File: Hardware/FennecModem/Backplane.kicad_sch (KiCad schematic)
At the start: 4 parts, among them U101 NCP1117-12_SOT223

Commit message: Bump backplane
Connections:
- new net SPI_CLK: U302.12 (SPI_CLK)
- new net SPI_SDA1: U302.14 (SPI_SDA1/SPI_SDI)
- new net SPI_SDA2: U302.16 (SPI_SDA2)
- new net SPI_SDA3: U302.18 (SPI_SDA3)
- new net SPI_SDA4: U302.20 (SPI_SDA4)
- no-connect marks 0 -> 7
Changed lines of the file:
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@@
   (junction (at 159.385 88.265) (diameter 0) (color 0 0 0 0)
   )
-  (junction (at 97.155 120.65) (diameter 0) (color 0 0 0 0)
+  (junction (at 97.155 134.62) (diameter 0) (color 0 0 0 0)
   )
   (junction (at 172.72 98.425) (diameter 0) (color 0 0 0 0)
   )
-  (wire (pts (xy 97.155 118.745) (xy 97.155 120.65))
+  (no_connect (at 112.395 122.555))
+  (no_connect (at 112.395 90.805))
+  (no_connect (at 81.915 95.885))
+  (no_connect (at 112.395 93.345))
+  (no_connect (at 81.915 93.345))
+  (no_connect (at 112.395 95.885))
+  (no_connect (at 81.915 90.805))
+  (wire (pts (xy 97.155 132.715) (xy 97.155 134.62))
     (stroke (width 0) (type default))
   )
@@
     (stroke (width 0) (type default))
   )
-  (wire (pts (xy 112.395 93.345) (xy 114.935 93.345))
-    (stroke (width 0) (type default))
-  )
   (wire (pts (xy 159.385 88.265) (xy 159.385 90.805))
     (stroke (width 0) (type default))
   )
-  (wire (pts (xy 99.695 120.65) (xy 99.695 118.745))
+  (wire (pts (xy 112.395 114.935) (xy 114.935 114.935))
+    (stroke (width 0) (type default))
+  )
+  (wire (pts (xy 99.695 134.62) (xy 99.695 132.715))
     (stroke (width 0) (type default))
   )
@@
     (stroke (width 0) (type default))
   )
-  (wire (pts (xy 97.155 120.65) (xy 94.615 120.65))
+  (wire (pts (xy 97.155 134.62) (xy 94.615 134.62))
     (stroke (width 0) (type default))
   )
@@
     (stroke (width 0) (type default))
   )
+  (wire (pts (xy 112.395 102.235) (xy 114.935 102.235))
+    (stroke (width 0) (type default))
+  )
+  (wire (pts (xy 112.395 120.015) (xy 114.935 120.015))
+    (stroke (width 0) (type default))
+  )
   (wire (pts (xy 97.155 76.835) (xy 97.155 80.645))
     (stroke (width 0) (type default))
@@
     (stroke (width 0) (type default))
   )
+  (wire (pts (xy 112.395 104.775) (xy 114.935 104.775))
+    (stroke (width 0) (type default))
+  )
   (wire (pts (xy 140.335 88.265) (xy 159.385 88.265))
     (stroke (width 0) (type default))
   )
-  (wire (pts (xy 112.395 95.885) (xy 114.935 95.885))
-    (stroke (width 0) (type default))
-  )
-  (wire (pts (xy 97.155 120.65) (xy 99.695 120.65))
-    (stroke (width 0) (type default))
-  )
-  (wire (pts (xy 97.155 121.285) (xy 97.155 120.65))
+  (wire (pts (xy 112.395 117.475) (xy 114.935 117.475))
+    (stroke (width 0) (type default))
+  )
+  (wire (pts (xy 112.395 112.395) (xy 114.935 112.395))
+    (stroke (width 0) (type default))
+  )
+  (wire (pts (xy 97.155 134.62) (xy 99.695 134.62))
+    (stroke (width 0) (type default))
+  )
+  (wire (pts (xy 97.155 135.255) (xy 97.155 134.62))
     (stroke (width 0) (type default))
   )
@@
     (stroke (width 0) (type default))
   )
+  (wire (pts (xy 112.395 109.855) (xy 114.935 109.855))
+    (stroke (width 0) (type default))
+  )
   (wire (pts (xy 172.72 98.425) (xy 184.785 98.425))
     (stroke (width 0) (type default))
   )
-  (wire (pts (xy 94.615 118.745) (xy 94.615 120.65))
+  (wire (pts (xy 94.615 132.715) (xy 94.615 134.62))
     (stroke (width 0) (type default))
   )
@@
     (effects (font (size 1.27 1.27)) (justify right bottom))
   )
-  (hierarchical_label "I2C_SCL" (shape input) (at 114.935 93.345 0) (fields_autoplaced)
-    (effects (font (size 1.27 1.27)) (justify left))
-  )
-  (hierarchical_label "I2C_SDA" (shape bidirectional) (at 114.935 95.885 0) (fields_autoplaced)
+  (hierarchical_label "SPI_SDA3" (shape bidirectional) (at 114.935 117.475 0) (fields_autoplaced)
+    (effects (font (size 1.27 1.27)) (justify left))
+  )
+  (hierarchical_label "SPI_SDA2" (shape bidirectional) (at 114.935 114.935 0) (fields_autoplaced)
+    (effects (font (size 1.27 1.27)) (justify left))
+  )
+  (hierarchical_label "SPI_SDA1" (shape bidirectional) (at 114.935 112.395 0) (fields_autoplaced)
+    (effects (font (size 1.27 1.27)) (justify left))
+  )
+  (hierarchical_label "SPI_SDA4" (shape bidirectional) (at 114.935 120.015 0) (fields_autoplaced)
+    (effects (font (size 1.27 1.27)) (justify left))
+  )
+  (hierarchical_label "I2C_SDA" (shape bidirectional) (at 114.935 104.775 0) (fields_autoplaced)
+    (effects (font (size 1.27 1.27)) (justify left))
+  )
+  (hierarchical_label "SPI_CLK" (shape input) (at 114.935 109.855 0) (fields_autoplaced)
+    (effects (font (size 1.27 1.27)) (justify left))
+  )
+  (hierarchical_label "I2C_SCL" (shape input) (at 114.935 102.235 0) (fields_autoplaced)
     (effects (font (size 1.27 1.27)) (justify left))
   )
@@
     )
   )
-  (symbol (lib_id "power:GND") (at 97.155 121.285 0) (unit 1)
+  (symbol (lib_id "power:GND") (at 97.155 135.255 0) (unit 1)
     (in_bom yes) (on_board yes) (dnp no)
-    (property "Reference" "#PWR0116" (at 97.155 127.635 0)
-      (effects (font (size 1.27 1.27)) hide)
-    )
-    (property "Value" "GND" (at 97.155 125.095 0)
+    (property "Reference" "#PWR0116" (at 97.155 141.605 0)
+      (effects (font (size 1.27 1.27)) hide)
+    )
+    (property "Value" "GND" (at 97.155 139.065 0)
       (effects (font (size 1.27 1.27)))
     )
-    (property "Footprint" "" (at 97.155 121.285 0)
-      (effects (font (size 1.27 1.27)) hide)
-    )
-    (property "Datasheet" "" (at 97.155 121.285 0)
+    (property "Footprint" "" (at 97.155 135.255 0)
+      (effects (font (size 1.27 1.27)) hide)
+    )
+    (property "Datasheet" "" (at 97.155 135.255 0)
       (effects (font (size 1.27 1.27)) hide)
     )
@@
     )
     (pin "1")
+    (pin "10")
     (pin "11")
+    (pin "12")
     (pin "13")
+    (pin "14")
     (pin "15")
+    (pin "16")
+    (pin "17")
+    (pin "18")
     (pin "2")
+    (pin "20")
     (pin "3")
     (pin "30")
     (pin "4")
+    (pin "5")
+    (pin "6")
+    (pin "7")
+    (pin "8")
+    (pin "9")
     (instances
       (project "FennecModem"

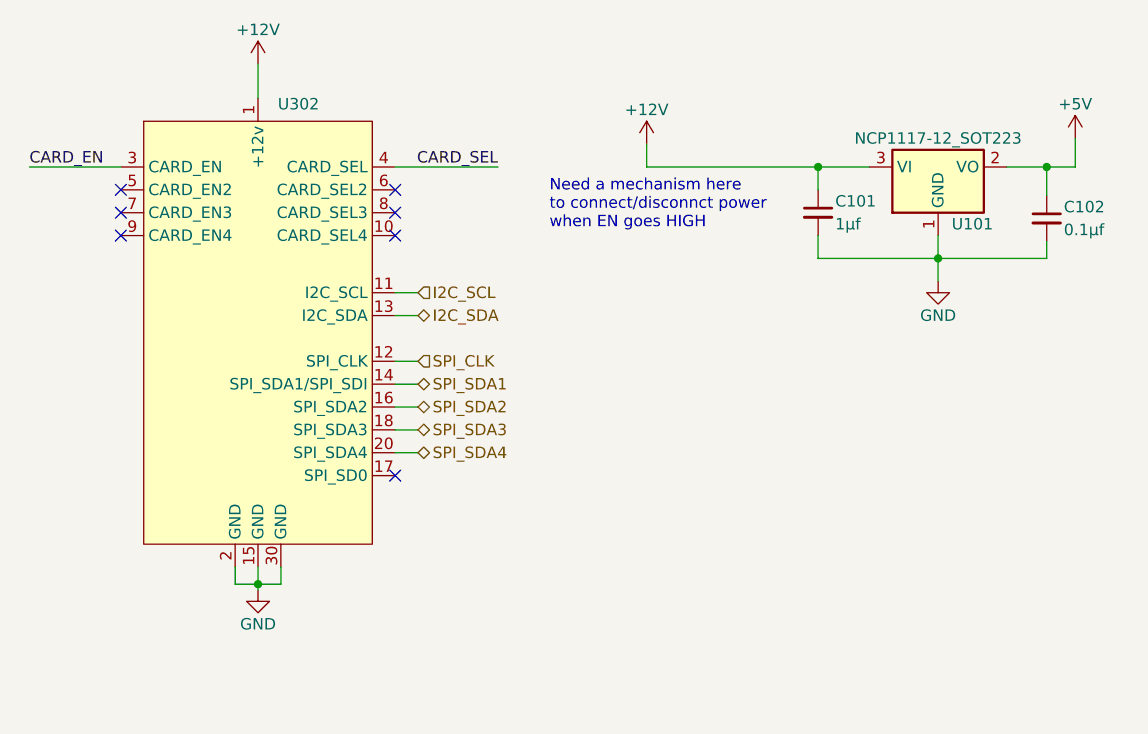
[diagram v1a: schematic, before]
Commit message: Bump everything with new backplane design
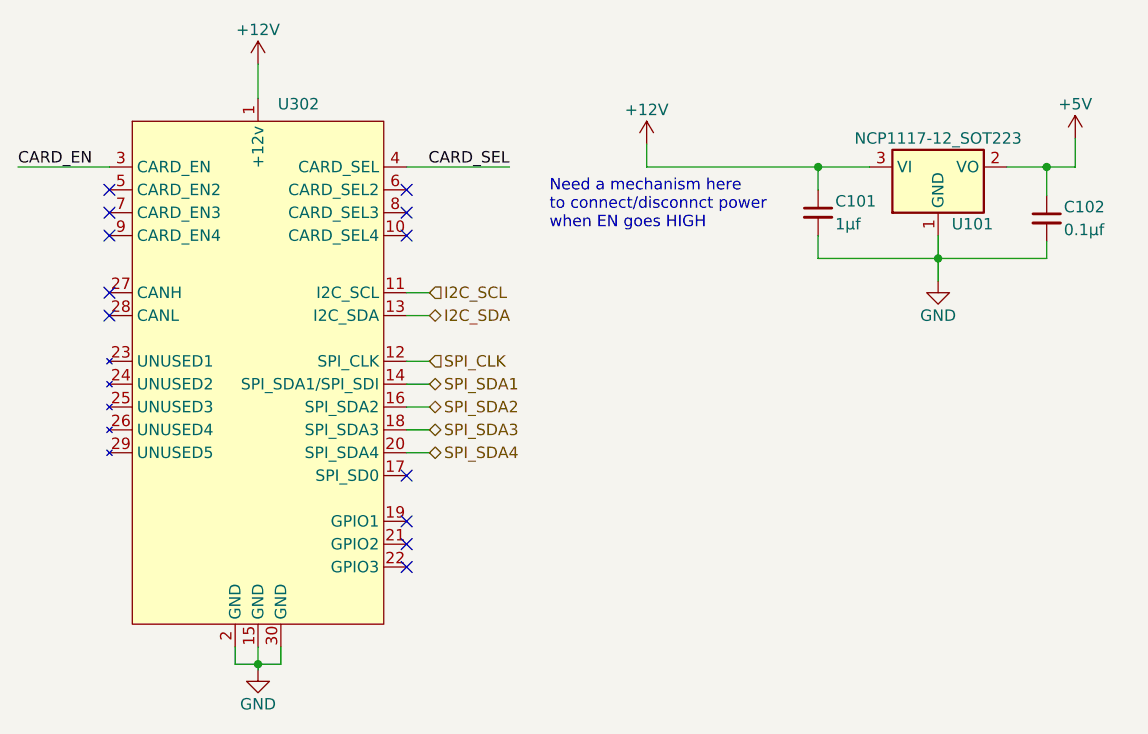
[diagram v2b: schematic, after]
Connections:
- no-connect marks 7 -> 12
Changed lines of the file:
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@@
   (junction (at 159.385 88.265) (diameter 0) (color 0 0 0 0)
   )
-  (junction (at 97.155 134.62) (diameter 0) (color 0 0 0 0)
+  (junction (at 97.155 143.51) (diameter 0) (color 0 0 0 0)
   )
   (junction (at 172.72 98.425) (diameter 0) (color 0 0 0 0)
   )
-  (no_connect (at 112.395 122.555))
-  (no_connect (at 112.395 90.805))
-  (no_connect (at 81.915 95.885))
-  (no_connect (at 112.395 93.345))
-  (no_connect (at 81.915 93.345))
-  (no_connect (at 112.395 95.885))
-  (no_connect (at 81.915 90.805))
-  (wire (pts (xy 97.155 132.715) (xy 97.155 134.62))
+  (no_connect (at 113.665 122.555))
+  (no_connect (at 80.645 104.775))
+  (no_connect (at 113.665 130.175))
+  (no_connect (at 113.665 90.805))
+  (no_connect (at 80.645 102.235))
+  (no_connect (at 80.645 95.885))
+  (no_connect (at 113.665 93.345))
+  (no_connect (at 80.645 93.345))
+  (no_connect (at 113.665 127.635))
+  (no_connect (at 113.665 95.885))
+  (no_connect (at 113.665 132.715))
+  (no_connect (at 80.645 90.805))
+  (wire (pts (xy 97.155 141.605) (xy 97.155 143.51))
     (stroke (width 0) (type default))
   )
@@
     (stroke (width 0) (type default))
   )
-  (wire (pts (xy 71.755 88.265) (xy 81.915 88.265))
+  (wire (pts (xy 70.485 88.265) (xy 80.645 88.265))
     (stroke (width 0) (type default))
   )
@@
     (stroke (width 0) (type default))
   )
-  (wire (pts (xy 112.395 114.935) (xy 114.935 114.935))
-    (stroke (width 0) (type default))
-  )
-  (wire (pts (xy 99.695 134.62) (xy 99.695 132.715))
+  (wire (pts (xy 113.665 114.935) (xy 116.205 114.935))
+    (stroke (width 0) (type default))
+  )
+  (wire (pts (xy 99.695 143.51) (xy 99.695 141.605))
     (stroke (width 0) (type default))
   )
@@
     (stroke (width 0) (type default))
   )
-  (wire (pts (xy 97.155 134.62) (xy 94.615 134.62))
+  (wire (pts (xy 97.155 143.51) (xy 94.615 143.51))
     (stroke (width 0) (type default))
   )
@@
     (stroke (width 0) (type default))
   )
-  (wire (pts (xy 112.395 102.235) (xy 114.935 102.235))
-    (stroke (width 0) (type default))
-  )
-  (wire (pts (xy 112.395 120.015) (xy 114.935 120.015))
+  (wire (pts (xy 113.665 102.235) (xy 116.205 102.235))
+    (stroke (width 0) (type default))
+  )
+  (wire (pts (xy 113.665 120.015) (xy 116.205 120.015))
     (stroke (width 0) (type default))
   )
@@
     (stroke (width 0) (type default))
   )
-  (wire (pts (xy 112.395 104.775) (xy 114.935 104.775))
+  (wire (pts (xy 113.665 104.775) (xy 116.205 104.775))
     (stroke (width 0) (type default))
   )
@@
     (stroke (width 0) (type default))
   )
-  (wire (pts (xy 112.395 117.475) (xy 114.935 117.475))
-    (stroke (width 0) (type default))
-  )
-  (wire (pts (xy 112.395 112.395) (xy 114.935 112.395))
-    (stroke (width 0) (type default))
-  )
-  (wire (pts (xy 97.155 134.62) (xy 99.695 134.62))
-    (stroke (width 0) (type default))
-  )
-  (wire (pts (xy 97.155 135.255) (xy 97.155 134.62))
-    (stroke (width 0) (type default))
-  )
-  (wire (pts (xy 123.825 88.265) (xy 112.395 88.265))
+  (wire (pts (xy 113.665 117.475) (xy 116.205 117.475))
+    (stroke (width 0) (type default))
+  )
+  (wire (pts (xy 113.665 112.395) (xy 116.205 112.395))
+    (stroke (width 0) (type default))
+  )
+  (wire (pts (xy 97.155 143.51) (xy 99.695 143.51))
+    (stroke (width 0) (type default))
+  )
+  (wire (pts (xy 97.155 144.145) (xy 97.155 143.51))
+    (stroke (width 0) (type default))
+  )
+  (wire (pts (xy 125.095 88.265) (xy 113.665 88.265))
     (stroke (width 0) (type default))
   )
@@
     (stroke (width 0) (type default))
   )
-  (wire (pts (xy 112.395 109.855) (xy 114.935 109.855))
+  (wire (pts (xy 113.665 109.855) (xy 116.205 109.855))
     (stroke (width 0) (type default))
   )
@@
     (stroke (width 0) (type default))
   )
-  (wire (pts (xy 94.615 132.715) (xy 94.615 134.62))
+  (wire (pts (xy 94.615 141.605) (xy 94.615 143.51))
     (stroke (width 0) (type default))
   )
@@
     (effects (font (size 1.27 1.27)) (justify left bottom))
   )
-  (label "CARD_EN" (at 71.755 88.265 0) (fields_autoplaced)
+  (label "CARD_EN" (at 70.485 88.265 0) (fields_autoplaced)
     (effects (font (size 1.27 1.27)) (justify left bottom))
   )
-  (label "CARD_SEL" (at 123.825 88.265 180) (fields_autoplaced)
+  (label "CARD_SEL" (at 125.095 88.265 180) (fields_autoplaced)
     (effects (font (size 1.27 1.27)) (justify right bottom))
   )
-  (hierarchical_label "SPI_SDA3" (shape bidirectional) (at 114.935 117.475 0) (fields_autoplaced)
-    (effects (font (size 1.27 1.27)) (justify left))
-  )
-  (hierarchical_label "SPI_SDA2" (shape bidirectional) (at 114.935 114.935 0) (fields_autoplaced)
-    (effects (font (size 1.27 1.27)) (justify left))
-  )
-  (hierarchical_label "SPI_SDA1" (shape bidirectional) (at 114.935 112.395 0) (fields_autoplaced)
-    (effects (font (size 1.27 1.27)) (justify left))
-  )
-  (hierarchical_label "SPI_SDA4" (shape bidirectional) (at 114.935 120.015 0) (fields_autoplaced)
-    (effects (font (size 1.27 1.27)) (justify left))
-  )
-  (hierarchical_label "I2C_SDA" (shape bidirectional) (at 114.935 104.775 0) (fields_autoplaced)
-    (effects (font (size 1.27 1.27)) (justify left))
-  )
-  (hierarchical_label "SPI_CLK" (shape input) (at 114.935 109.855 0) (fields_autoplaced)
-    (effects (font (size 1.27 1.27)) (justify left))
-  )
-  (hierarchical_label "I2C_SCL" (shape input) (at 114.935 102.235 0) (fields_autoplaced)
+  (hierarchical_label "SPI_SDA3" (shape bidirectional) (at 116.205 117.475 0) (fields_autoplaced)
+    (effects (font (size 1.27 1.27)) (justify left))
+  )
+  (hierarchical_label "SPI_SDA2" (shape bidirectional) (at 116.205 114.935 0) (fields_autoplaced)
+    (effects (font (size 1.27 1.27)) (justify left))
+  )
+  (hierarchical_label "SPI_SDA1" (shape bidirectional) (at 116.205 112.395 0) (fields_autoplaced)
+    (effects (font (size 1.27 1.27)) (justify left))
+  )
+  (hierarchical_label "SPI_SDA4" (shape bidirectional) (at 116.205 120.015 0) (fields_autoplaced)
+    (effects (font (size 1.27 1.27)) (justify left))
+  )
+  (hierarchical_label "I2C_SDA" (shape bidirectional) (at 116.205 104.775 0) (fields_autoplaced)
+    (effects (font (size 1.27 1.27)) (justify left))
+  )
+  (hierarchical_label "SPI_CLK" (shape input) (at 116.205 109.855 0) (fields_autoplaced)
+    (effects (font (size 1.27 1.27)) (justify left))
+  )
+  (hierarchical_label "I2C_SCL" (shape input) (at 116.205 102.235 0) (fields_autoplaced)
     (effects (font (size 1.27 1.27)) (justify left))
   )
@@
     )
   )
-  (symbol (lib_id "power:GND") (at 97.155 135.255 0) (unit 1)
+  (symbol (lib_id "power:GND") (at 97.155 144.145 0) (unit 1)
     (in_bom yes) (on_board yes) (dnp no)
-    (property "Reference" "#PWR0116" (at 97.155 141.605 0)
-      (effects (font (size 1.27 1.27)) hide)
-    )
-    (property "Value" "GND" (at 97.155 139.065 0)
+    (property "Reference" "#PWR0116" (at 97.155 150.495 0)
+      (effects (font (size 1.27 1.27)) hide)
+    )
+    (property "Value" "GND" (at 97.155 147.955 0)
       (effects (font (size 1.27 1.27)))
     )
-    (property "Footprint" "" (at 97.155 135.255 0)
-      (effects (font (size 1.27 1.27)) hide)
-    )
-    (property "Datasheet" "" (at 97.155 135.255 0)
+    (property "Footprint" "" (at 97.155 144.145 0)
+      (effects (font (size 1.27 1.27)) hide)
+    )
+    (property "Datasheet" "" (at 97.155 144.145 0)
       (effects (font (size 1.27 1.27)) hide)
     )
@@
     (pin "17")
     (pin "18")
+    (pin "19")
     (pin "2")
     (pin "20")
+    (pin "21")
+    (pin "22")
+    (pin "23")
+    (pin "24")
+    (pin "25")
+    (pin "26")
+    (pin "27")
+    (pin "28")
+    (pin "29")
     (pin "3")
     (pin "30")

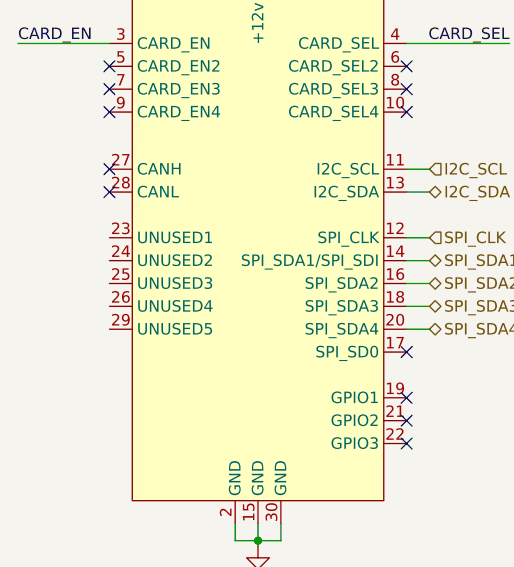
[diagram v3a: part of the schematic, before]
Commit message: Include new chip! 3v3 system from now on..
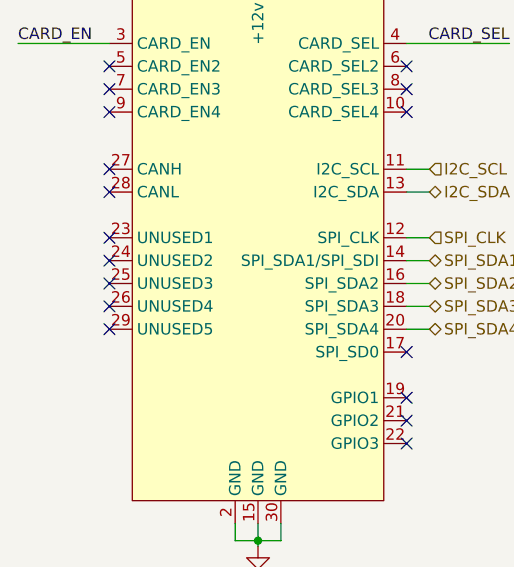
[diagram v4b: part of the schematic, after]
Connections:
- no-connect marks 12 -> 17
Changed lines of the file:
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@@
   (no_connect (at 113.665 122.555))
   (no_connect (at 80.645 104.775))
+  (no_connect (at 80.645 120.015))
   (no_connect (at 113.665 130.175))
   (no_connect (at 113.665 90.805))
+  (no_connect (at 80.645 109.855))
   (no_connect (at 80.645 102.235))
   (no_connect (at 80.645 95.885))
   (no_connect (at 113.665 93.345))
+  (no_connect (at 80.645 114.935))
+  (no_connect (at 80.645 117.475))
+  (no_connect (at 80.645 112.395))
   (no_connect (at 80.645 93.345))
   (no_connect (at 113.665 127.635))
@@
   (symbol (lib_id "power:+12V") (at 97.155 76.835 0) (unit 1)
     (in_bom yes) (on_board yes) (dnp no)
-    (property "Reference" "#PWR0117" (at 97.155 80.645 0)
+    (property "Reference" "#PWR0308" (at 97.155 80.645 0)
       (effects (font (size 1.27 1.27)) hide)
     )
@@
     (instances
       (project "FennecModem"
-        (path "/8cb1f8f8-0f28-4c6f-8a0b-e6b064917aa9"
-          (reference "#PWR0117") (unit 1)
-        )
         (path "/8cb1f8f8-0f28-4c6f-8a0b-e6b064917aa9/192ed9e7-ecb8-4622-a83a-67936d551760"
           (reference "#PWR0308") (unit 1)
@@
   (symbol (lib_id "power:GND") (at 97.155 144.145 0) (unit 1)
     (in_bom yes) (on_board yes) (dnp no)
-    (property "Reference" "#PWR0116" (at 97.155 150.495 0)
+    (property "Reference" "#PWR0307" (at 97.155 150.495 0)
       (effects (font (size 1.27 1.27)) hide)
     )
@@
     (instances
       (project "FennecModem"
-        (path "/8cb1f8f8-0f28-4c6f-8a0b-e6b064917aa9"
-          (reference "#PWR0116") (unit 1)
-        )
         (path "/8cb1f8f8-0f28-4c6f-8a0b-e6b064917aa9/192ed9e7-ecb8-4622-a83a-67936d551760"
           (reference "#PWR0307") (unit 1)
@@
       )
       (project "FennecModem"
-        (path "/8cb1f8f8-0f28-4c6f-8a0b-e6b064917aa9"
-          (reference "C107") (unit 1)
-        )
         (path "/8cb1f8f8-0f28-4c6f-8a0b-e6b064917aa9/192ed9e7-ecb8-4622-a83a-67936d551760"
           (reference "C303") (unit 1)
@@
       )
       (project "FennecModem"
-        (path "/8cb1f8f8-0f28-4c6f-8a0b-e6b064917aa9"
-          (reference "C106") (unit 1)
-        )
         (path "/8cb1f8f8-0f28-4c6f-8a0b-e6b064917aa9/192ed9e7-ecb8-4622-a83a-67936d551760"
           (reference "C302") (unit 1)
@@
       )
       (project "FennecModem"
-        (path "/8cb1f8f8-0f28-4c6f-8a0b-e6b064917aa9"
-          (reference "U102") (unit 1)
-        )
         (path "/8cb1f8f8-0f28-4c6f-8a0b-e6b064917aa9/192ed9e7-ecb8-4622-a83a-67936d551760"
           (reference "U301") (unit 1)
@@
   (symbol (lib_id "power:+12V") (at 140.335 85.725 0) (unit 1)
     (in_bom yes) (on_board yes) (dnp no)
-    (property "Reference" "#PWR0132" (at 140.335 89.535 0)
+    (property "Reference" "#PWR0304" (at 140.335 89.535 0)
       (effects (font (size 1.27 1.27)) hide)
     )
@@
     (instances
       (project "FennecModem"
-        (path "/8cb1f8f8-0f28-4c6f-8a0b-e6b064917aa9"
-          (reference "#PWR0132") (unit 1)
-        )
         (path "/8cb1f8f8-0f28-4c6f-8a0b-e6b064917aa9/192ed9e7-ecb8-4622-a83a-67936d551760"
           (reference "#PWR0304") (unit 1)
@@
       )
       (project "FennecModem"
-        (path "/8cb1f8f8-0f28-4c6f-8a0b-e6b064917aa9"
-          (reference "#PWR0130") (unit 1)
-        )
         (path "/8cb1f8f8-0f28-4c6f-8a0b-e6b064917aa9/192ed9e7-ecb8-4622-a83a-67936d551760"
           (reference "#PWR0305") (unit 1)
@@
       )
       (project "FennecModem"
-        (path "/8cb1f8f8-0f28-4c6f-8a0b-e6b064917aa9"
-          (reference "#PWR0131") (unit 1)
-        )
         (path "/8cb1f8f8-0f28-4c6f-8a0b-e6b064917aa9/192ed9e7-ecb8-4622-a83a-67936d551760"
           (reference "#PWR0306") (unit 1)
